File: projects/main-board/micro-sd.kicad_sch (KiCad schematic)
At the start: 4 parts

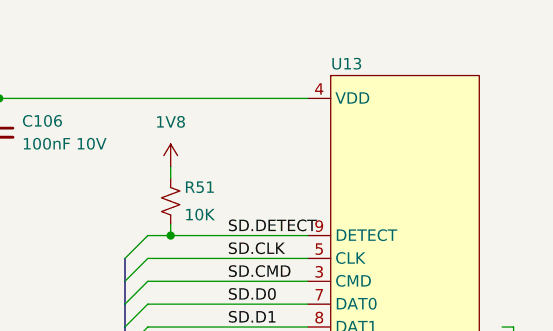
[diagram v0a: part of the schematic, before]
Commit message: Updated schematics with new symbols
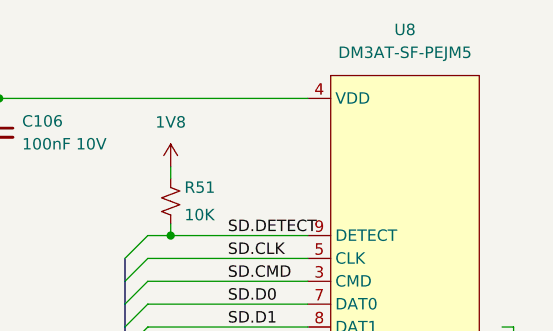
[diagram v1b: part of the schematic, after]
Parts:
- removed U13: ~, symbol symbol-library:DM3AT-SF-PEJM5
- added U8: DM3AT-SF-PEJM5, footprint-library:DM3AT-SF-PEJM5, symbol symbol-library:DM3AT-SF-PEJM5
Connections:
- net 3V3: now also U8.4 (VDD)
- net SD.CLK: now also U8.5 (CLK)
- net SD.CMD: now also U8.3 (CMD)
- net SD.D0: now also U8.7 (DAT0)
- net SD.D1: now also U8.8 (DAT1)
- net SD.D2: now also U8.1 (DAT2)
- net SD.D3: now also U8.2 (CD/DAT3)
- net SD.DETECT: now also U8.9 (DETECT)
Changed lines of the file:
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@@
+	)
+	(symbol
+		(lib_name "DM3AT-SF-PEJM5_1")
+		(lib_id "symbol-library:DM3AT-SF-PEJM5")
+		(at 161.29 80.01 0)
+		(unit 1)
+		(exclude_from_sim no)
+		(in_bom yes)
+		(on_board yes)
+		(dnp no)
+		(fields_autoplaced yes)
+		(property "Reference" "U8"
+			(at 169.545 74.93 0)
+			(effects
+				(font
+					(size 1.27 1.27)
+				)
+			)
+		)
+		(property "Value" "DM3AT-SF-PEJM5"
+			(at 169.545 77.47 0)
+			(effects
+				(font
+					(size 1.27 1.27)
+				)
+			)
+		)
+		(property "Footprint" "footprint-library:DM3AT-SF-PEJM5"
+			(at 175.006 117.348 0)
+			(effects
+				(font
+					(size 1.27 1.27)
+				)
+				(hide yes)
+			)
+		)
+		(property "Datasheet" ""
+			(at 161.29 80.01 0)
+			(effects
+				(font
+					(size 1.27 1.27)
+				)
+				(hide yes)
+			)
+		)
+		(property "Description" ""
+			(at 161.29 80.01 0)
+			(effects
+				(font
+					(size 1.27 1.27)
+				)
+				(hide yes)
+			)
+		)
+		(pin "1"
+		)
+		(pin "2"
+		)
+		(pin "6"
+		)
+		(pin "4"
+		)
+		(pin "9"
+		)
+		(pin "5"
+		)
+		(pin "3"
+		)
+		(pin "7"
+		)
+		(pin "8"
+		)
+		(instances
+			(project ""
+				(path "/c621b5fd-2ef7-4a67-960d-0ffc72b1245a/78e3df9a-9d0e-4599-9dc1-8d07bc071d30"
+					(reference "U8")
+					(unit 1)
+				)
+			)
+		)
 	)
 	(symbol
@@
 					(unit 1)
 				)
-			)
-		)
-	)
-	(symbol
-		(lib_id "symbol-library:DM3AT-SF-PEJM5")
-		(at 161.29 80.01 0)
-		(unit 1)
-		(exclude_from_sim no)
-		(in_bom yes)
-		(on_board yes)
-		(dnp no)
-		(property "Reference" "U13"
-			(at 163.068 78.74 0)
-			(effects
-				(font
-					(size 1.27 1.27)
-				)
-			)
-		)
-		(property "Value" "~"
-			(at 167.386 78.994 0)
-			(effects
-				(font
-					(size 1.27 1.27)
-				)
-			)
-		)
-		(property "Footprint" ""
-			(at 161.29 80.01 0)
-			(effects
-				(font
-					(size 1.27 1.27)
-				)
-				(hide yes)
-			)
-		)
-		(property "Datasheet" ""
-			(at 161.29 80.01 0)
-			(effects
-				(font
-					(size 1.27 1.27)
-				)
-				(hide yes)
-			)
-		)
-		(property "Description" ""
-			(at 161.29 80.01 0)
-			(effects
-				(font
-					(size 1.27 1.27)
-				)
-				(hide yes)
-			)
-		)
-		(pin "3"
-		)
-		(pin "7"
-		)
-		(pin "5"
-		)
-		(pin "1"
-		)
-		(pin "2"
-		)
-		(pin "8"
-		)
-		(pin "6"
-		)
-		(pin "4"
-		)
-		(pin "9"
-		)
-		(instances
-			(project ""
-				(path "/c621b5fd-2ef7-4a67-960d-0ffc72b1245a/78e3df9a-9d0e-4599-9dc1-8d07bc071d30"
-					(reference "U13")
-					(unit 1)
-				)

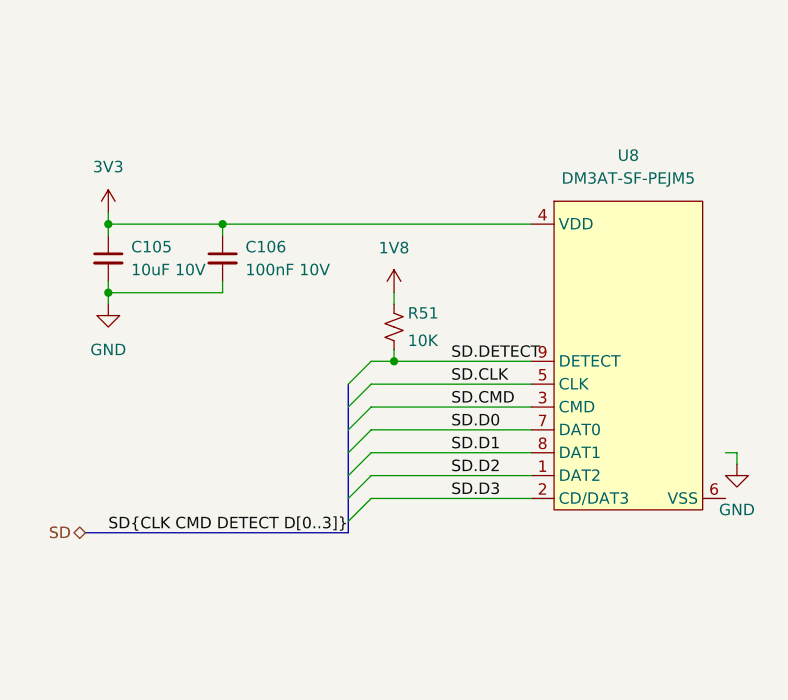
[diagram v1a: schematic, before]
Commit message: Re-annotate schematics.
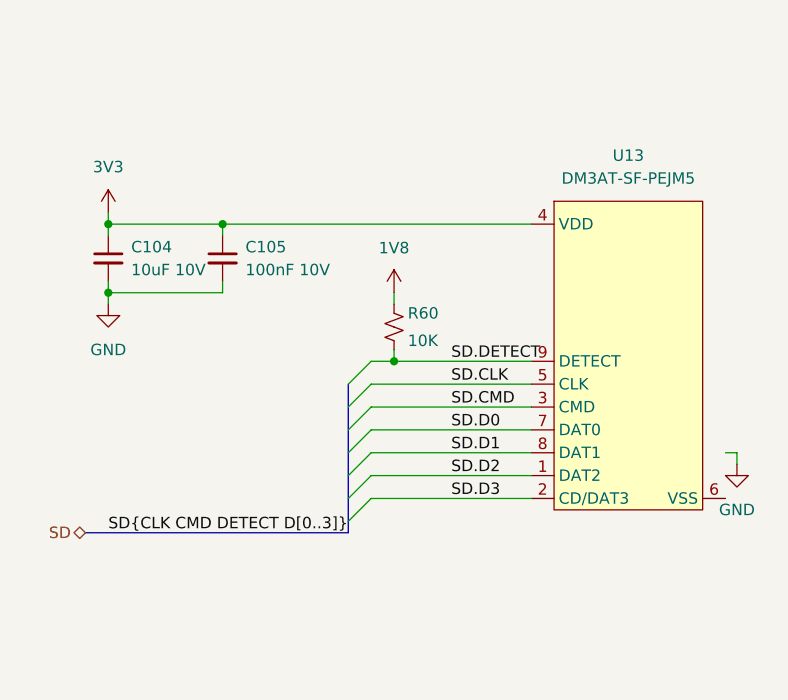
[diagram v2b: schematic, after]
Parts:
- renumbered C105 to C104, C106 to C105, R51 to R60, U8 to U13
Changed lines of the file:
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@@
 		(dnp no)
 		(fields_autoplaced yes)
-		(property "Reference" "#PWR0138"
+		(property "Reference" "#PWR0149"
 			(at 111.76 85.09 0)
 			(effects
@@
 			(project ""
 				(path "/c621b5fd-2ef7-4a67-960d-0ffc72b1245a/78e3df9a-9d0e-4599-9dc1-8d07bc071d30"
-					(reference "#PWR0138")
+					(reference "#PWR0149")
 					(unit 1)
 				)
@@
 		(dnp no)
 		(fields_autoplaced yes)
-		(property "Reference" "C106"
+		(property "Reference" "C105"
 			(at 127 85.0962 0)
 			(effects
@@
 			(project "main-board"
 				(path "/c621b5fd-2ef7-4a67-960d-0ffc72b1245a/78e3df9a-9d0e-4599-9dc1-8d07bc071d30"
-					(reference "C106")
+					(reference "C105")
 					(unit 1)
 				)
@@
 		(dnp no)
 		(fields_autoplaced yes)
-		(property "Reference" "#PWR0139"
+		(property "Reference" "#PWR0152"
 			(at 181.61 115.57 0)
 			(effects
@@
 			(project ""
 				(path "/c621b5fd-2ef7-4a67-960d-0ffc72b1245a/78e3df9a-9d0e-4599-9dc1-8d07bc071d30"
-					(reference "#PWR0139")
+					(reference "#PWR0152")
 					(unit 1)
 				)
@@
 		(dnp no)
 		(fields_autoplaced yes)
-		(property "Reference" "U8"
+		(property "Reference" "U13"
 			(at 169.545 74.93 0)
 			(effects
@@
 			(project ""
 				(path "/c621b5fd-2ef7-4a67-960d-0ffc72b1245a/78e3df9a-9d0e-4599-9dc1-8d07bc071d30"
-					(reference "U8")
+					(reference "U13")
 					(unit 1)
 				)
@@
 		(dnp no)
 		(fields_autoplaced yes)
-		(property "Reference" "#PWR089"
+		(property "Reference" "#PWR0151"
 			(at 143.51 93.98 0)
 			(effects
@@
 			(project "main-board"
 				(path "/c621b5fd-2ef7-4a67-960d-0ffc72b1245a/78e3df9a-9d0e-4599-9dc1-8d07bc071d30"
-					(reference "#PWR089")
+					(reference "#PWR0151")
 					(unit 1)
 				)
@@
 		(on_board yes)
 		(dnp no)
-		(property "Reference" "R51"
+		(property "Reference" "R60"
 			(at 145.034 92.456 0)
 			(effects
@@
 			(project ""
 				(path "/c621b5fd-2ef7-4a67-960d-0ffc72b1245a/78e3df9a-9d0e-4599-9dc1-8d07bc071d30"
-					(reference "R51")
+					(reference "R60")
 					(unit 1)
 				)
@@
 		(dnp no)
 		(fields_autoplaced yes)
-		(property "Reference" "#PWR0140"
+		(property "Reference" "#PWR0150"
 			(at 111.76 97.79 0)
 			(effects
@@
 			(project "main-board"
 				(path "/c621b5fd-2ef7-4a67-960d-0ffc72b1245a/78e3df9a-9d0e-4599-9dc1-8d07bc071d30"
-					(reference "#PWR0140")
+					(reference "#PWR0150")
 					(unit 1)
 				)
@@
 		(dnp no)
 		(fields_autoplaced yes)
-		(property "Reference" "C105"
+		(property "Reference" "C104"
 			(at 114.3 85.0962 0)
 			(effects
@@
 			(project ""
 				(path "/c621b5fd-2ef7-4a67-960d-0ffc72b1245a/78e3df9a-9d0e-4599-9dc1-8d07bc071d30"
-					(reference "C105")
-					(unit 1)
-				)
+					(reference "C104")
+					(unit 1)
+				)

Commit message: Normalise capacitors
- Add capacitor parts to library.
- Replace all placeholder capacitors
  with the actual part numbers.
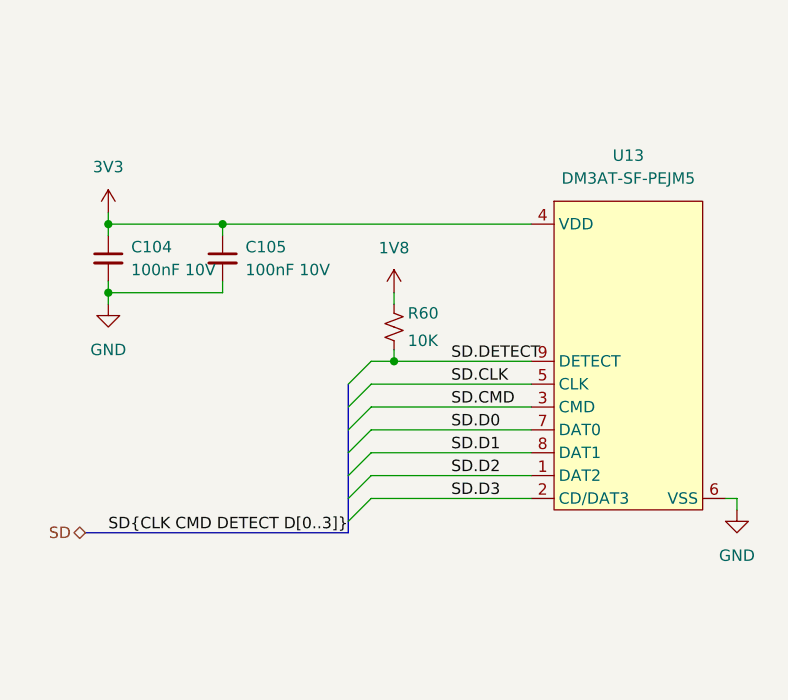
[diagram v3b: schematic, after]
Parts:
- removed C104: 10uF 10V, symbol Device:C_Small
- removed C105: 100nF 10V, symbol Device:C_Small
- added C104, C105: 100nF 10V, Capacitor_SMD:C_0402_1005Metric, symbol symbol-library-capacitors:CC0402KRX7R6BB104
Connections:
- net 3V3: now also C104.1, C105.1
- net GND: now also U13.6 (VSS), C104.2, C105.2
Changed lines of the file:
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@@
 	(wire
 		(pts
-			(xy 180.34 107.95) (xy 181.61 107.95)
+			(xy 180.34 113.03) (xy 181.61 113.03)
 		)
 		(stroke
@@
 	(wire
 		(pts
-			(xy 181.61 107.95) (xy 181.61 109.22)
+			(xy 181.61 113.03) (xy 181.61 114.3)
 		)
 		(stroke
@@
 		(dnp no)
 		(fields_autoplaced yes)
-		(property "Reference" "#PWR0149"
+		(property "Reference" "#PWR0147"
 			(at 111.76 85.09 0)
 			(effects
@@
 			(project ""
 				(path "/c621b5fd-2ef7-4a67-960d-0ffc72b1245a/78e3df9a-9d0e-4599-9dc1-8d07bc071d30"
-					(reference "#PWR0149")
+					(reference "#PWR0147")
 					(unit 1)
 				)
@@
 	)
 	(symbol
-		(lib_id "Device:C_Small")
+		(lib_id "power:GND")
+		(at 181.61 114.3 0)
+		(unit 1)
+		(exclude_from_sim no)
+		(in_bom yes)
+		(on_board yes)
+		(dnp no)
+		(fields_autoplaced yes)
+		(property "Reference" "#PWR0150"
+			(at 181.61 120.65 0)
+			(effects
+				(font
+					(size 1.27 1.27)
+				)
+				(hide yes)
+			)
+		)
+		(property "Value" "GND"
+			(at 181.61 119.38 0)
+			(effects
+				(font
+					(size 1.27 1.27)
+				)
+			)
+		)
+		(property "Footprint" ""
+			(at 181.61 114.3 0)
+			(effects
+				(font
+					(size 1.27 1.27)
+				)
+				(hide yes)
+			)
+		)
+		(property "Datasheet" ""
+			(at 181.61 114.3 0)
+			(effects
+				(font
+					(size 1.27 1.27)
+				)
+				(hide yes)
+			)
+		)
+		(property "Description" "Power symbol creates a global label with name \"GND\" , ground"
+			(at 181.61 114.3 0)
+			(effects
+				(font
+					(size 1.27 1.27)
+				)
+				(hide yes)
+			)
+		)
+		(pin "1"
+		)
+		(instances
+			(project ""
+				(path "/c621b5fd-2ef7-4a67-960d-0ffc72b1245a/78e3df9a-9d0e-4599-9dc1-8d07bc071d30"
+					(reference "#PWR0150")
+					(unit 1)
+				)
+			)
+		)
+	)
+	(symbol
+		(lib_id "symbol-library-capacitors:CC0402KRX7R6BB104")
 		(at 124.46 86.36 0)
 		(unit 1)
@@
 			)
 		)
-		(property "Footprint" ""
+		(property "Footprint" "Capacitor_SMD:C_0402_1005Metric"
 			(at 124.46 86.36 0)
 			(effects
@@
 				(path "/c621b5fd-2ef7-4a67-960d-0ffc72b1245a/78e3df9a-9d0e-4599-9dc1-8d07bc071d30"
 					(reference "C105")
-					(unit 1)
-				)
-			)
-		)
-	)
-	(symbol
-		(lib_id "power:GND")
-		(at 181.61 109.22 0)
-		(unit 1)
-		(exclude_from_sim no)
-		(in_bom yes)
-		(on_board yes)
-		(dnp no)
-		(fields_autoplaced yes)
-		(property "Reference" "#PWR0152"
-			(at 181.61 115.57 0)
-			(effects
-				(font
-					(size 1.27 1.27)
-				)
-				(hide yes)
-			)
-		)
-		(property "Value" "GND"
-			(at 181.61 114.3 0)
-			(effects
-				(font
-					(size 1.27 1.27)
-				)
-			)
-		)
-		(property "Footprint" ""
-			(at 181.61 109.22 0)
-			(effects
-				(font
-					(size 1.27 1.27)
-				)
-				(hide yes)
-			)
-		)
-		(property "Datasheet" ""
-			(at 181.61 109.22 0)
-			(effects
-				(font
-					(size 1.27 1.27)
-				)
-				(hide yes)
-			)
-		)
-		(property "Description" "Power symbol creates a global label with name \"GND\" , ground"
-			(at 181.61 109.22 0)
-			(effects
-				(font
-					(size 1.27 1.27)
-				)
-				(hide yes)
-			)
-		)
-		(pin "1"
-		)
-		(instances
-			(project ""
-				(path "/c621b5fd-2ef7-4a67-960d-0ffc72b1245a/78e3df9a-9d0e-4599-9dc1-8d07bc071d30"
-					(reference "#PWR0152")
 					(unit 1)
 				)
@@
 		(dnp no)
 		(fields_autoplaced yes)
-		(property "Reference" "#PWR0151"
+		(property "Reference" "#PWR0149"
 			(at 143.51 93.98 0)
 			(effects
@@
 			(project "main-board"
 				(path "/c621b5fd-2ef7-4a67-960d-0ffc72b1245a/78e3df9a-9d0e-4599-9dc1-8d07bc071d30"
-					(reference "#PWR0151")
+					(reference "#PWR0149")
 					(unit 1)
 				)
@@
 	)
 	(symbol
-		(lib_id "power:GND")
-		(at 111.76 91.44 0)
-		(unit 1)
-		(exclude_from_sim no)
-		(in_bom yes)
-		(on_board yes)
-		(dnp no)
-		(fields_autoplaced yes)
-		(property "Reference" "#PWR0150"
-			(at 111.76 97.79 0)
-			(effects
-				(font
-					(size 1.27 1.27)
-				)
-				(hide yes)
-			)
-		)
-		(property "Value" "GND"
-			(at 111.76 96.52 0)
-			(effects
-				(font
-					(size 1.27 1.27)
-				)
-			)
-		)
-		(property "Footprint" ""
-			(at 111.76 91.44 0)
-			(effects
-				(font
-					(size 1.27 1.27)
-				)
-				(hide yes)
-			)
-		)
-		(property "Datasheet" ""
-			(at 111.76 91.44 0)
-			(effects
-				(font
-					(size 1.27 1.27)
-				)
-				(hide yes)
-			)
-		)
-		(property "Description" "Power symbol creates a global label with name \"GND\" , ground"
-			(at 111.76 91.44 0)
-			(effects
-				(font
-					(size 1.27 1.27)
-				)
-				(hide yes)
-			)
-		)
-		(pin "1"
-		)
-		(instances
-			(project "main-board"
-				(path "/c621b5fd-2ef7-4a67-960d-0ffc72b1245a/78e3df9a-9d0e-4599-9dc1-8d07bc071d30"
-					(reference "#PWR0150")
-					(unit 1)
-				)
-			)
-		)
-	)
-	(symbol
-		(lib_id "Device:C_Small")
+		(lib_id "symbol-library-capacitors:CC0402KRX7R6BB104")
 		(at 111.76 86.36 0)
 		(unit 1)
@@
 			)
 		)
-		(property "Value" "10uF 10V"
+		(property "Value" "100nF 10V"
 			(at 114.3 87.6362 0)
 			(effects
@@
 			)
 		)
-		(property "Footprint" ""
+		(property "Footprint" "Capacitor_SMD:C_0402_1005Metric"
 			(at 111.76 86.36 0)
 			(effects
@@
 		)
 		(instances
-			(project ""
+			(project "main-board"
 				(path "/c621b5fd-2ef7-4a67-960d-0ffc72b1245a/78e3df9a-9d0e-4599-9dc1-8d07bc071d30"
 					(reference "C104")
 					(unit 1)
 				)
+			)
+		)
+	)
+	(symbol
+		(lib_id "power:GND")
+		(at 111.76 91.44 0)
+		(unit 1)
+		(exclude_from_sim no)
+		(in_bom yes)
+		(on_board yes)
+		(dnp no)
+		(fields_autoplaced yes)
+		(property "Reference" "#PWR0148"
+			(at 111.76 97.79 0)
+			(effects
+				(font
+					(size 1.27 1.27)
+				)
+				(hide yes)
+			)
+		)
+		(property "Value" "GND"
+			(at 111.76 96.52 0)
+			(effects
+				(font
+					(size 1.27 1.27)
+				)
+			)
+		)
+		(property "Footprint" ""
+			(at 111.76 91.44 0)
+			(effects
+				(font
+					(size 1.27 1.27)
+				)
+				(hide yes)
+			)
+		)
+		(property "Datasheet" ""
+			(at 111.76 91.44 0)
+			(effects
+				(font
+					(size 1.27 1.27)
+				)
+				(hide yes)
+			)
+		)
+		(property "Description" "Power symbol creates a global label with name \"GND\" , ground"
+			(at 111.76 91.44 0)
+			(effects
+				(font
+					(size 1.27 1.27)
+				)
+				(hide yes)
+			)
+		)
+		(pin "1"
+		)
+		(instances
+			(project "main-board"
+				(path "/c621b5fd-2ef7-4a67-960d-0ffc72b1245a/78e3df9a-9d0e-4599-9dc1-8d07bc071d30"
+					(reference "#PWR0148")
+					(unit 1)
+				)

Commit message: Replace placeholder resistors
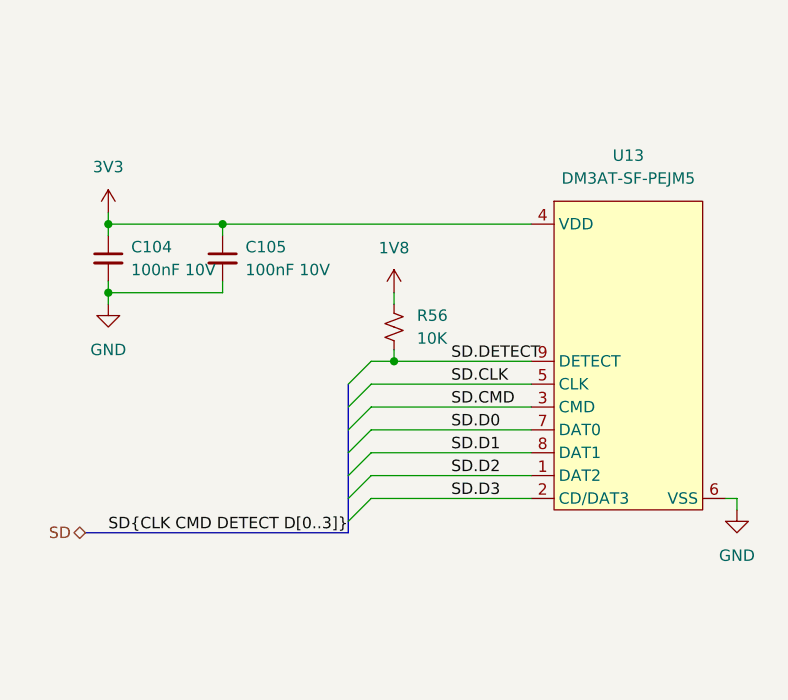
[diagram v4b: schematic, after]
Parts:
- removed R60: 10K, symbol Device:R_Small_US
- added R56: 10K, Resistor_SMD:R_0402_1005Metric, symbol symbol-library-resistors:RC0402JR-0710KL
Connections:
- net 1V8: now also R56.1
- net SD.DETECT: now also R56.2
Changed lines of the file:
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@@
+	)
+	(symbol
+		(lib_id "symbol-library-resistors:RC0402JR-0710KL")
+		(at 143.51 93.98 0)
+		(unit 1)
+		(exclude_from_sim no)
+		(in_bom yes)
+		(on_board yes)
+		(dnp no)
+		(fields_autoplaced yes)
+		(property "Reference" "R56"
+			(at 146.05 92.7099 0)
+			(effects
+				(font
+					(size 1.27 1.27)
+				)
+				(justify left)
+			)
+		)
+		(property "Value" "10K"
+			(at 146.05 95.2499 0)
+			(effects
+				(font
+					(size 1.27 1.27)
+				)
+				(justify left)
+			)
+		)
+		(property "Footprint" "Resistor_SMD:R_0402_1005Metric"
+			(at 143.51 93.98 0)
+			(effects
+				(font
+					(size 1.27 1.27)
+				)
+				(hide yes)
+			)
+		)
+		(property "Datasheet" "~"
+			(at 143.51 93.98 0)
+			(effects
+				(font
+					(size 1.27 1.27)
+				)
+				(hide yes)
+			)
+		)
+		(property "Description" "Resistor, small US symbol"
+			(at 143.51 93.98 0)
+			(effects
+				(font
+					(size 1.27 1.27)
+				)
+				(hide yes)
+			)
+		)
+		(pin "1"
+		)
+		(pin "2"
+		)
+		(instances
+			(project "main-board"
+				(path "/c621b5fd-2ef7-4a67-960d-0ffc72b1245a/78e3df9a-9d0e-4599-9dc1-8d07bc071d30"
+					(reference "R56")
+					(unit 1)
+				)
+			)
+		)
 	)
 	(symbol
@@
 					(unit 1)
 				)
-			)
-		)
-	)
-	(symbol
-		(lib_id "Device:R_Small_US")
-		(at 143.51 93.98 0)
-		(unit 1)
-		(exclude_from_sim no)
-		(in_bom yes)
-		(on_board yes)
-		(dnp no)
-		(property "Reference" "R60"
-			(at 145.034 92.456 0)
-			(effects
-				(font
-					(size 1.27 1.27)
-				)
-				(justify left)
-			)
-		)
-		(property "Value" "10K"
-			(at 145.034 95.504 0)
-			(effects
-				(font
-					(size 1.27 1.27)
-				)
-				(justify left)
-			)
-		)
-		(property "Footprint" ""
-			(at 143.51 93.98 0)
-			(effects
-				(font
-					(size 1.27 1.27)
-				)
-				(hide yes)
-			)
-		)
-		(property "Datasheet" "~"
-			(at 143.51 93.98 0)
-			(effects
-				(font
-					(size 1.27 1.27)
-				)
-				(hide yes)
-			)
-		)
-		(property "Description" "Resistor, small US symbol"
-			(at 143.51 93.98 0)
-			(effects
-				(font
-					(size 1.27 1.27)
-				)
-				(hide yes)
-			)
-		)
-		(pin "1"
-		)
-		(pin "2"
-		)
-		(instances
-			(project ""
-				(path "/c621b5fd-2ef7-4a67-960d-0ffc72b1245a/78e3df9a-9d0e-4599-9dc1-8d07bc071d30"
-					(reference "R60")
-					(unit 1)
-				)
